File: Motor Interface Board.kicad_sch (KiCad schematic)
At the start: 12 parts, among them J1 Conn_02x04_Counter_Clockwise, J2 Conn_02x04_Counter_Clockwise, J3 Conn_01x02_Pin, J4 Conn_01x02_Pin, J5 Conn_01x20, J6 Conn_01x20, J7 Conn_02x04_Odd_Even, U1 TXB0108PW

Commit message: Update J1/J2 to be 2x5, route PU- through A1/B1 and GP1
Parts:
- removed J2: Conn_02x04_Counter_Clockwise, symbol Connector_Generic:Conn_02x04_Counter_Clockwise
- added J2: Conn_02x04_Counter_Clockwise, symbol Connector_Generic:Conn_02x05_Counter_Clockwise
- J1: symbol Connector_Generic:Conn_02x04_Counter_Clockwise -> Connector_Generic:Conn_02x05_Counter_Clockwise
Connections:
- net DR-: now also U1.17 (B3), J2.3 (Pin_3); no longer U1.18 (B2)
- net DR-_3V3: now also U1.4 (A3); no longer U1.3 (A2)
- net GND: now also J1.10 (Pin_10), J1.9 (Pin_9), J2.10 (Pin_10), J2.6 (Pin_6), J2.7 (Pin_7), J2.8 (Pin_8), J2.9 (Pin_9); no longer J1.5 (Pin_5)
- net MF-: now also U1.16 (B4), J2.4 (Pin_4); no longer U1.17 (B3)
- net MF-_3V3: now also U1.5 (A4); no longer U1.4 (A3)
- net PU-: now also U1.20 (B1), J2.2 (Pin_2); no longer U1.12 (B8)
- net PU-_3V3: now also J5.2 (Pin_2), U1.1 (A1); no longer J5.9 (Pin_9), U1.9 (A8)
- net XCOM: now also U1.18 (B2), J2.1 (Pin_1); no longer U1.20 (B1)
- net XCOM_3V3: now also U1.3 (A2); no longer U1.1 (A1)
- new net M_GND: J1.5 (Pin_5), J2.5 (Pin_5)

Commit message: Source +5V from either VBUS or +5V_IN
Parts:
- added R2, R3: 0, symbol Device:R_Small
- J1, J2: value Conn_02x04_Counter_Clockwise -> Conn_02x05_Counter_Clockwise
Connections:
- net M_GND is gone; now on net GND: J1.5 (Pin_5), J2.5 (Pin_5)
- net +5V: now also R2.1, R3.2; no longer D1.1 (K), J6.2 (Pin_2)
- net +5V_IN: now also R3.1
- net at J6.1 (Pin_1): now also R2.2
- new net: D1.1 (K), J6.2 (Pin_2)
- no-connect marks 30 -> 29
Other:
- note added: "Motor (Green) GND"
- note added: "PCB GND"
- note added: "PSU GND"
- moved on the sheet: J3

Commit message: Layout placement
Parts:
- C1, C2: footprint (none) -> Capacitor_SMD:C_0805_2012Metric_Pad1.18x1.45mm_HandSolder
- J1, J2: value Conn_02x05_Counter_Clockwise -> Conn_02x05_Odd_Even; footprint (none) -> Connector_PinHeader_2.54mm:PinHeader_2x05_P2.54mm_Vertical; symbol Connector_Generic:Conn_02x05_Counter_Clockwise -> Connector_Generic:Conn_02x05_Odd_Even
- R2, R3: footprint (none) -> Resistor_SMD:R_0805_2012Metric_Pad1.20x1.40mm_HandSolder
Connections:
- net DR-: now also J1.5 (Pin_5), J2.5 (Pin_5); no longer J1.3 (Pin_3), J2.3 (Pin_3)
- net GND: now also J1.2 (Pin_2), J1.4 (Pin_4), J2.2 (Pin_2), J2.4 (Pin_4); no longer J1.5 (Pin_5), J1.7 (Pin_7), J2.5 (Pin_5), J2.7 (Pin_7)
- net MF-: now also J1.7 (Pin_7), J2.7 (Pin_7); no longer J1.4 (Pin_4), J2.4 (Pin_4)
- net PU-: now also J1.3 (Pin_3), J2.3 (Pin_3); no longer J1.2 (Pin_2), J2.2 (Pin_2)
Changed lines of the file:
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@@
 			)
 		)
-		(property "Footprint" ""
+		(property "Footprint" "Resistor_SMD:R_0805_2012Metric_Pad1.20x1.40mm_HandSolder"
 			(at 177.8 27.94 0)
 			(hide yes)
@@
 			)
 		)
-		(property "Footprint" ""
+		(property "Footprint" "Resistor_SMD:R_0805_2012Metric_Pad1.20x1.40mm_HandSolder"
 			(at 195.58 27.94 0)
 			(hide yes)
@@
 			)
 		)
-		(property "Footprint" ""
+		(property "Footprint" "Capacitor_SMD:C_0805_2012Metric_Pad1.18x1.45mm_HandSolder"
 			(at 72.39 26.67 0)
 			(hide yes)
@@
 			)
 		)
-		(property "Footprint" ""
+		(property "Footprint" "Capacitor_SMD:C_0805_2012Metric_Pad1.18x1.45mm_HandSolder"
 			(at 92.71 26.67 0)
 			(hide yes)
@@
 	)
 	(symbol
-		(lib_id "Connector_Generic:Conn_02x05_Counter_Clockwise")
+		(lib_id "Connector_Generic:Conn_02x05_Odd_Even")
 		(at 36.83 69.85 0)
 		(unit 1)
@@
 			)
 		)
-		(property "Value" "Conn_02x05_Counter_Clockwise"
+		(property "Value" "Conn_02x05_Odd_Even"
 			(at 38.1 60.96 0)
 			(show_name no)
@@
 			)
 		)
-		(property "Footprint" ""
+		(property "Footprint" "Connector_PinHeader_2.54mm:PinHeader_2x05_P2.54mm_Vertical"
 			(at 36.83 69.85 0)
 			(hide yes)
@@
 			)
 		)
-		(property "Description" "Generic connector, double row, 02x05, counter clockwise pin numbering scheme (similar to DIP package numbering), script generated (kicad-library-utils/schlib/autogen/connector/)"
+		(property "Description" "Generic connector, double row, 02x05, odd/even pin numbering scheme (row 1 odd numbers, row 2 even numbers), script generated (kicad-library-utils/schlib/autogen/connector/)"
 			(at 36.83 69.85 0)
 			(hide yes)
@@
 	)
 	(symbol
-		(lib_id "Connector_Generic:Conn_02x05_Counter_Clockwise")
+		(lib_id "Connector_Generic:Conn_02x05_Odd_Even")
 		(at 36.83 41.91 0)
 		(unit 1)
@@
 			)
 		)
-		(property "Value" "Conn_02x05_Counter_Clockwise"
+		(property "Value" "Conn_02x05_Odd_Even"
 			(at 38.1 33.02 0)
 			(show_name no)
@@
 			)
 		)
-		(property "Footprint" ""
+		(property "Footprint" "Connector_PinHeader_2.54mm:PinHeader_2x05_P2.54mm_Vertical"
 			(at 36.83 41.91 0)
 			(hide yes)
@@
 			)
 		)
-		(property "Description" "Generic connector, double row, 02x05, counter clockwise pin numbering scheme (similar to DIP package numbering), script generated (kicad-library-utils/schlib/autogen/connector/)"
+		(property "Description" "Generic connector, double row, 02x05, odd/even pin numbering scheme (row 1 odd numbers, row 2 even numbers), script generated (kicad-library-utils/schlib/autogen/connector/)"
 			(at 36.83 41.91 0)
 			(hide yes)

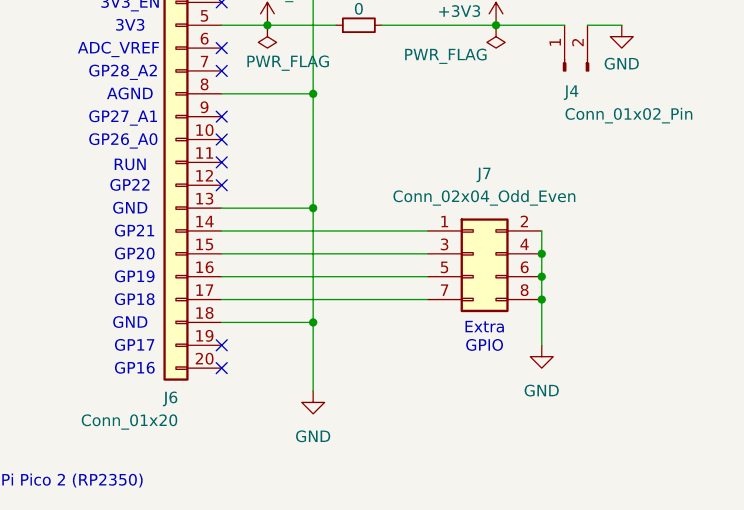
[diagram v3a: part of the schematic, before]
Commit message: Add mounting holes + reconfigure GPIO to use SPI capable pins
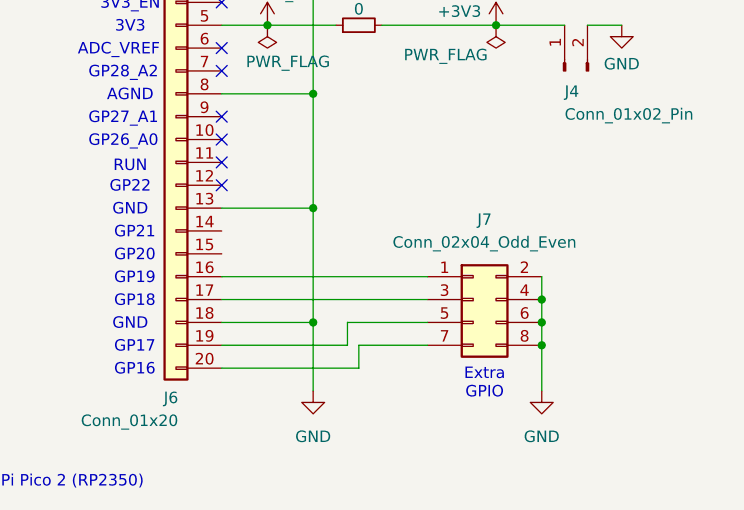
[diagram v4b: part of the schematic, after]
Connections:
- net at J6.14 (Pin_14): no longer J7.1 (Pin_1)
- net at J6.15 (Pin_15): no longer J7.3 (Pin_3)
- net at J6.16 (Pin_16): now also J7.1 (Pin_1); no longer J7.5 (Pin_5)
- net at J6.17 (Pin_17): now also J7.3 (Pin_3); no longer J7.7 (Pin_7)
- net at J6.19 (Pin_19): now also J7.5 (Pin_5)
- net at J6.20 (Pin_20): now also J7.7 (Pin_7)
- no-connect marks 29 -> 27
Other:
- moved on the sheet: J7
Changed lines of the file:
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@@
 	(text "Extra\nGPIO"
 		(exclude_from_sim no)
-		(at 204.47 76.708 0)
+		(at 204.47 81.788 0)
 		(effects
 			(font
@@
 	)
 	(junction
-		(at 210.82 72.39)
+		(at 210.82 77.47)
 		(diameter 0)
 		(color 0 0 0 0)
@@
 	)
 	(junction
-		(at 210.82 67.31)
+		(at 210.82 72.39)
 		(diameter 0)
 		(color 0 0 0 0)
@@
 	)
 	(junction
-		(at 210.82 69.85)
+		(at 210.82 74.93)
 		(diameter 0)
 		(color 0 0 0 0)
@@
 	)
 	(no_connect
-		(at 175.26 77.47)
-	)
-	(no_connect
 		(at 132.08 67.31)
 	)
@@
 	)
 	(no_connect
-		(at 175.26 80.01)
-	)
-	(no_connect
 		(at 175.26 59.69)
 	)
@@
 	(wire
 		(pts
+			(xy 175.26 80.01) (xy 190.5 80.01)
+		)
+		(stroke
+			(width 0)
+			(type default)
+		)
+	)
+	(wire
+		(pts
 			(xy 82.55 64.77) (xy 82.55 68.58)
 		)
@@
 	(wire
 		(pts
+			(xy 189.23 74.93) (xy 198.12 74.93)
+		)
+		(stroke
+			(width 0)
+			(type default)
+		)
+	)
+	(wire
+		(pts
 			(xy 85.09 26.67) (xy 85.09 29.21)
 		)
@@
 	(wire
 		(pts
-			(xy 92.71 44.45) (xy 96.52 44.45)
+			(xy 175.26 77.47) (xy 189.23 77.47)
 		)
 		(stroke
@@
 	(wire
 		(pts
-			(xy 175.26 67.31) (xy 198.12 67.31)
+			(xy 92.71 44.45) (xy 96.52 44.45)
 		)
 		(stroke
@@
 	(wire
 		(pts
-			(xy 210.82 67.31) (xy 210.82 69.85)
+			(xy 210.82 72.39) (xy 210.82 74.93)
 		)
 		(stroke
@@
 	(wire
 		(pts
+			(xy 189.23 77.47) (xy 189.23 74.93)
+		)
+		(stroke
+			(width 0)
+			(type default)
+		)
+	)
+	(wire
+		(pts
 			(xy 85.09 26.67) (xy 90.17 26.67)
 		)
@@
 	(wire
 		(pts
-			(xy 175.26 72.39) (xy 198.12 72.39)
+			(xy 205.74 41.91) (xy 213.36 41.91)
 		)
 		(stroke
@@
 	(wire
 		(pts
-			(xy 205.74 41.91) (xy 213.36 41.91)
+			(xy 119.38 82.55) (xy 119.38 74.93)
 		)
 		(stroke
@@
 	(wire
 		(pts
-			(xy 119.38 82.55) (xy 119.38 74.93)
+			(xy 44.45 64.77) (xy 44.45 67.31)
 		)
 		(stroke
@@
 	(wire
 		(pts
-			(xy 44.45 64.77) (xy 44.45 67.31)
+			(xy 44.45 69.85) (xy 44.45 72.39)
 		)
 		(stroke
@@
 	(wire
 		(pts
-			(xy 44.45 69.85) (xy 44.45 72.39)
+			(xy 210.82 74.93) (xy 210.82 77.47)
 		)
 		(stroke
@@
 	(wire
 		(pts
-			(xy 210.82 69.85) (xy 210.82 72.39)
+			(xy 80.01 26.67) (xy 80.01 29.21)
 		)
 		(stroke
@@
 	(wire
 		(pts
-			(xy 80.01 26.67) (xy 80.01 29.21)
+			(xy 185.42 36.83) (xy 175.26 36.83)
 		)
 		(stroke
@@
 	(wire
 		(pts
-			(xy 185.42 36.83) (xy 175.26 36.83)
+			(xy 175.26 69.85) (xy 198.12 69.85)
 		)
 		(stroke
@@
 	(wire
 		(pts
-			(xy 210.82 72.39) (xy 210.82 77.47)
+			(xy 210.82 77.47) (xy 210.82 82.55)
 		)
 		(stroke
@@
 	(wire
 		(pts
-			(xy 175.26 69.85) (xy 198.12 69.85)
+			(xy 68.58 39.37) (xy 72.39 39.37)
 		)
 		(stroke
@@
 	(wire
 		(pts
-			(xy 68.58 39.37) (xy 72.39 39.37)
+			(xy 44.45 67.31) (xy 44.45 69.85)
 		)
 		(stroke
@@
 	(wire
 		(pts
-			(xy 44.45 67.31) (xy 44.45 69.85)
+			(xy 175.26 72.39) (xy 198.12 72.39)
 		)
 		(stroke
@@
 	(wire
 		(pts
-			(xy 210.82 64.77) (xy 210.82 67.31)
+			(xy 210.82 69.85) (xy 210.82 72.39)
 		)
 		(stroke
@@
 	(wire
 		(pts
-			(xy 175.26 64.77) (xy 198.12 64.77)
+			(xy 186.69 27.94) (xy 193.04 27.94)
 		)
 		(stroke
@@
 	(wire
 		(pts
-			(xy 186.69 27.94) (xy 193.04 27.94)
+			(xy 68.58 46.99) (xy 72.39 46.99)
 		)
 		(stroke
@@
 	(wire
 		(pts
-			(xy 68.58 46.99) (xy 72.39 46.99)
+			(xy 44.45 39.37) (xy 44.45 41.91)
 		)
 		(stroke
@@
 	(wire
 		(pts
-			(xy 44.45 39.37) (xy 44.45 41.91)
+			(xy 44.45 74.93) (xy 44.45 77.47)
 		)
 		(stroke
@@
 	(wire
 		(pts
-			(xy 44.45 74.93) (xy 44.45 77.47)
+			(xy 190.5 77.47) (xy 198.12 77.47)
 		)
 		(stroke
@@
 	(wire
 		(pts
+			(xy 190.5 80.01) (xy 190.5 77.47)
+		)
+		(stroke
+			(width 0)
+			(type default)
+		)
+	)
+	(wire
+		(pts
 			(xy 130.81 34.29) (xy 132.08 34.29)
 		)
@@
 	(symbol
 		(lib_id "power:GND")
-		(at 210.82 77.47 0)
+		(at 210.82 82.55 0)
 		(unit 1)
 		(body_style 1)
@@
 		(fields_autoplaced yes)
 		(property "Reference" "#PWR015"
-			(at 210.82 83.82 0)
+			(at 210.82 88.9 0)
 			(hide yes)
 			(show_name no)
@@
 		)
 		(property "Value" "GND"
-			(at 210.82 82.55 0)
+			(at 210.82 87.63 0)
 			(show_name no)
 			(do_not_autoplace no)
@@
 		)
 		(property "Footprint" ""
-			(at 210.82 77.47 0)
+			(at 210.82 82.55 0)
 			(hide yes)
 			(show_name no)
@@
 		)
 		(property "Datasheet" ""
-			(at 210.82 77.47 0)
+			(at 210.82 82.55 0)
 			(hide yes)
 			(show_name no)
@@
 		)
 		(property "Description" "Power symbol creates a global label with name \"GND\" , ground"
-			(at 210.82 77.47 0)
+			(at 210.82 82.55 0)
 			(hide yes)
 			(show_name no)
@@
 	(symbol
 		(lib_id "Connector_Generic:Conn_02x04_Odd_Even")
-		(at 203.2 67.31 0)
+		(at 203.2 72.39 0)
 		(unit 1)
 		(body_style 1)
@@
 		(fields_autoplaced yes)
 		(property "Reference" "J7"
-			(at 204.47 58.42 0)
+			(at 204.47 63.5 0)
 			(show_name no)
 			(do_not_autoplace no)
@@
 		)
 		(property "Value" "Conn_02x04_Odd_Even"
-			(at 204.47 60.96 0)
+			(at 204.47 66.04 0)
 			(show_name no)
 			(do_not_autoplace no)
@@
 		)
 		(property "Footprint" "Connector_PinHeader_2.54mm:PinHeader_2x04_P2.54mm_Vertical"
-			(at 203.2 67.31 0)
+			(at 203.2 72.39 0)
 			(hide yes)
 			(show_name no)
@@
 		)
 		(property "Datasheet" ""
-			(at 203.2 67.31 0)
+			(at 203.2 72.39 0)
 			(hide yes)
 			(show_name no)
@@
 		)
 		(property "Description" "Generic connector, double row, 02x04, odd/even pin numbering scheme (row 1 odd numbers, row 2 even numbers), script generated (kicad-library-utils/schlib/autogen/connector/)"
-			(at 203.2 67.31 0)
+			(at 203.2 72.39 0)
 			(hide yes)
 			(show_name no)
